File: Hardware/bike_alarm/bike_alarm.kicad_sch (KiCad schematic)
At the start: 4 parts, among them Q1 Q_NMOS_DGS, Y1 Piezo Buzzer

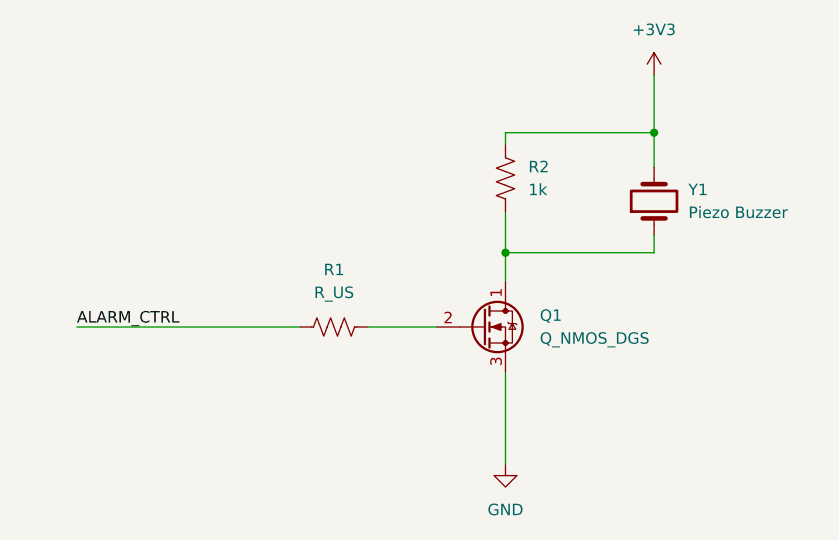
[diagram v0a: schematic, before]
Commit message: bike_alarm pcb update and bom
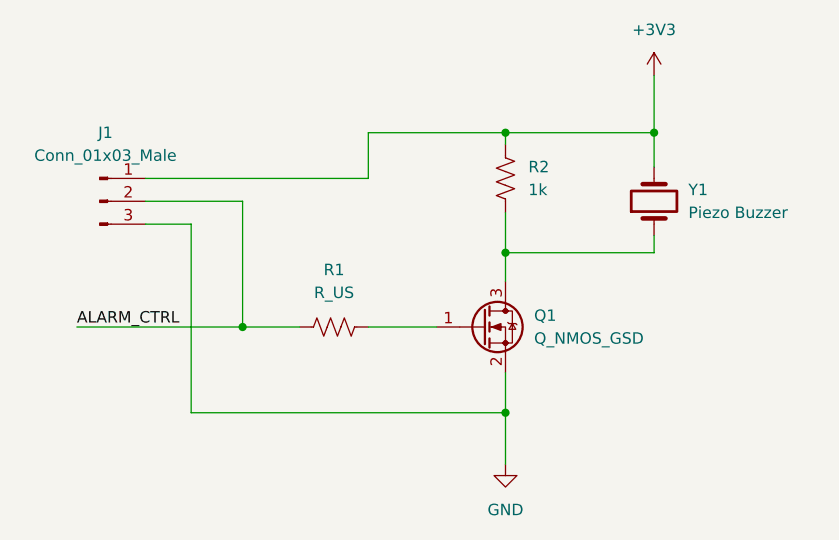
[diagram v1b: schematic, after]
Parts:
- removed Q1: Q_NMOS_DGS, Package_TO_SOT_SMD:SOT-23, symbol Device:Q_NMOS_DGS
- added J1: Conn_01x03_Male, Connector_PinHeader_2.54mm:PinHeader_1x03_P2.54mm_Vertical, symbol Connector:Conn_01x03_Male
- added Q1: Q_NMOS_GSD, Package_TO_SOT_SMD:SOT-23, symbol Device:Q_NMOS_GSD
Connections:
- net +3V3: now also J1.1 (Pin_1)
- net ALARM_CTRL: now also J1.2 (Pin_2)
- net GND: now also J1.3 (Pin_3), Q1.2 (S)
- net at R2.2, Y1.1: now also Q1.3 (D)
- net at R1.2: now also Q1.1 (G)
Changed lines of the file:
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@@
 (kicad_sch (version 20211123) (generator eeschema)
   (paper "A4")
+  (junction (at 81.28 108.585) (diameter 0) (color 0 0 0 0)
+  )
   (junction (at 81.28 90.805) (diameter 0) (color 0 0 0 0)
   )
+  (junction (at 52.07 99.06) (diameter 0) (color 0 0 0 0)
+  )
   (junction (at 97.79 77.47) (diameter 0) (color 0 0 0 0)
   )
-  (wire (pts (xy 81.28 104.14) (xy 81.28 114.3))
+  (junction (at 81.28 77.47) (diameter 0) (color 0 0 0 0)
+  )
+  (wire (pts (xy 41.275 87.63) (xy 46.355 87.63))
+    (stroke (width 0) (type default) (color 0 0 0 0))
+  )
+  (wire (pts (xy 41.275 85.09) (xy 52.07 85.09))
+    (stroke (width 0) (type default) (color 0 0 0 0))
+  )
+  (wire (pts (xy 41.275 82.55) (xy 66.04 82.55))
+    (stroke (width 0) (type default) (color 0 0 0 0))
+  )
+  (wire (pts (xy 81.28 104.14) (xy 81.28 108.585))
+    (stroke (width 0) (type default) (color 0 0 0 0))
+  )
+  (wire (pts (xy 52.07 85.09) (xy 52.07 99.06))
+    (stroke (width 0) (type default) (color 0 0 0 0))
+  )
+  (wire (pts (xy 46.355 108.585) (xy 81.28 108.585))
     (stroke (width 0) (type default) (color 0 0 0 0))
   )
@@
     (stroke (width 0) (type default) (color 0 0 0 0))
   )
+  (wire (pts (xy 81.28 108.585) (xy 81.28 114.3))
+    (stroke (width 0) (type default) (color 0 0 0 0))
+  )
   (wire (pts (xy 81.28 86.36) (xy 81.28 90.805))
     (stroke (width 0) (type default) (color 0 0 0 0))
   )
-  (wire (pts (xy 33.655 99.06) (xy 58.42 99.06))
+  (wire (pts (xy 33.655 99.06) (xy 52.07 99.06))
     (stroke (width 0) (type default) (color 0 0 0 0))
   )
@@
     (stroke (width 0) (type default) (color 0 0 0 0))
   )
+  (wire (pts (xy 52.07 99.06) (xy 58.42 99.06))
+    (stroke (width 0) (type default) (color 0 0 0 0))
+  )
+  (wire (pts (xy 66.04 77.47) (xy 81.28 77.47))
+    (stroke (width 0) (type default) (color 0 0 0 0))
+  )
   (wire (pts (xy 97.79 88.9) (xy 97.79 90.805))
     (stroke (width 0) (type default) (color 0 0 0 0))
   )
+  (wire (pts (xy 46.355 87.63) (xy 46.355 108.585))
+    (stroke (width 0) (type default) (color 0 0 0 0))
+  )
   (wire (pts (xy 81.28 77.47) (xy 97.79 77.47))
+    (stroke (width 0) (type default) (color 0 0 0 0))
+  )
+  (wire (pts (xy 66.04 82.55) (xy 66.04 77.47))
     (stroke (width 0) (type default) (color 0 0 0 0))
   )
@@
     (effects (font (size 1.27 1.27)) (justify left bottom))
   )
-  (symbol (lib_id "Device:Q_NMOS_DGS") (at 78.74 99.06 0) (unit 1)
-    (in_bom yes) (on_board yes) (fields_autoplaced)
-    (property "Reference" "Q1" (id 0) (at 85.09 97.7899 0)
-      (effects (font (size 1.27 1.27)) (justify left))
-    )
-    (property "Value" "Q_NMOS_DGS" (id 1) (at 85.09 100.3299 0)
+  (symbol (lib_id "Connector:Conn_01x03_Male") (at 36.195 85.09 0) (unit 1)
+    (in_bom yes) (on_board yes) (fields_autoplaced)
+    (property "Reference" "J1" (id 0) (at 36.83 77.47 0))
+    (property "Value" "Conn_01x03_Male" (id 1) (at 36.83 80.01 0))
+    (property "Footprint" "Connector_PinHeader_2.54mm:PinHeader_1x03_P2.54mm_Vertical" (id 2) (at 36.195 85.09 0)
+      (effects (font (size 1.27 1.27)) hide)
+    )
+    (property "Datasheet" "~" (id 3) (at 36.195 85.09 0)
+      (effects (font (size 1.27 1.27)) hide)
+    )
+    (pin "1")
+    (pin "2")
+    (pin "3")
+  )
+  (symbol (lib_id "Device:Q_NMOS_GSD") (at 78.74 99.06 0) (unit 1)
+    (in_bom yes) (on_board yes)
+    (property "Reference" "Q1" (id 0) (at 84.455 97.7899 0)
+      (effects (font (size 1.27 1.27)) (justify left))
+    )
+    (property "Value" "Q_NMOS_GSD" (id 1) (at 84.455 100.3299 0)
       (effects (font (size 1.27 1.27)) (justify left))
     )
@@
       (reference "#PWR0102") (unit 1) (value "GND") (footprint "")
     )
-    (path "/2d38429c-e76f-4ac3-a609-eca610b831a6"
-      (reference "Q1") (unit 1) (value "Q_NMOS_DGS") (footprint "Package_TO_SOT_SMD:SOT-23")
+    (path "/04c74dd5-f6c8-4c9d-8c28-3b17ac54986b"
+      (reference "J1") (unit 1) (value "Conn_01x03_Male") (footprint "Connector_PinHeader_2.54mm:PinHeader_1x03_P2.54mm_Vertical")
+    )
+    (path "/2da672a4-e8e8-42bd-b3a0-04b94e90287d"
+      (reference "Q1") (unit 1) (value "Q_NMOS_GSD") (footprint "Package_TO_SOT_SMD:SOT-23")
     )
     (path "/a1c19031-85a7-4245-9e0a-eed346ebf312"

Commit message: all boards pass DRC and have appropriate silkscreens, will order tomorrow
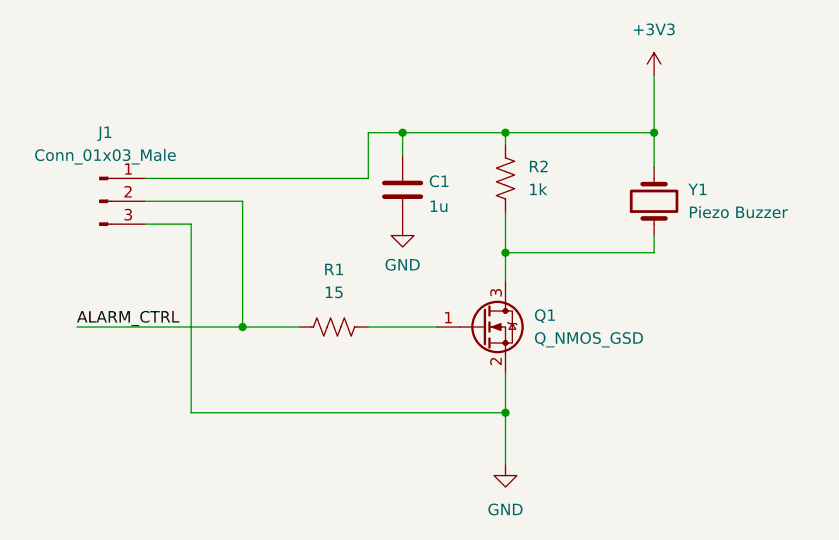
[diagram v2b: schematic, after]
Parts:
- added C1: 1u, Capacitor_SMD:C_0805_2012Metric, symbol Device:C
- R1: value R_US -> 15
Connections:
- net +3V3: now also C1.1
- net GND: now also C1.2
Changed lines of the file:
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@@
   (junction (at 81.28 77.47) (diameter 0) (color 0 0 0 0)
   )
+  (junction (at 69.85 77.47) (diameter 0) (color 0 0 0 0)
+  )
   (wire (pts (xy 41.275 87.63) (xy 46.355 87.63))
     (stroke (width 0) (type default) (color 0 0 0 0))
@@
     (stroke (width 0) (type default) (color 0 0 0 0))
   )
+  (wire (pts (xy 69.85 77.47) (xy 69.85 80.01))
+    (stroke (width 0) (type default) (color 0 0 0 0))
+  )
+  (wire (pts (xy 69.85 77.47) (xy 81.28 77.47))
+    (stroke (width 0) (type default) (color 0 0 0 0))
+  )
   (wire (pts (xy 97.79 77.47) (xy 97.79 81.28))
     (stroke (width 0) (type default) (color 0 0 0 0))
@@
     (stroke (width 0) (type default) (color 0 0 0 0))
   )
-  (wire (pts (xy 66.04 77.47) (xy 81.28 77.47))
+  (wire (pts (xy 66.04 77.47) (xy 69.85 77.47))
     (stroke (width 0) (type default) (color 0 0 0 0))
   )
@@
     (pin "3")
   )
+  (symbol (lib_id "power:GND") (at 69.85 87.63 0) (unit 1)
+    (in_bom yes) (on_board yes) (fields_autoplaced)
+    (property "Reference" "#PWR0103" (id 0) (at 69.85 93.98 0)
+      (effects (font (size 1.27 1.27)) hide)
+    )
+    (property "Value" "GND" (id 1) (at 69.85 92.1925 0))
+    (property "Footprint" "" (id 2) (at 69.85 87.63 0)
+      (effects (font (size 1.27 1.27)) hide)
+    )
+    (property "Datasheet" "" (id 3) (at 69.85 87.63 0)
+      (effects (font (size 1.27 1.27)) hide)
+    )
+    (pin "1")
+  )
   (symbol (lib_id "Device:Q_NMOS_GSD") (at 78.74 99.06 0) (unit 1)
     (in_bom yes) (on_board yes)
@@
     (pin "3")
   )
+  (symbol (lib_id "Device:C") (at 69.85 83.82 0) (unit 1)
+    (in_bom yes) (on_board yes) (fields_autoplaced)
+    (property "Reference" "C1" (id 0) (at 72.771 82.9115 0)
+      (effects (font (size 1.27 1.27)) (justify left))
+    )
+    (property "Value" "1u" (id 1) (at 72.771 85.6866 0)
+      (effects (font (size 1.27 1.27)) (justify left))
+    )
+    (property "Footprint" "Capacitor_SMD:C_0805_2012Metric" (id 2) (at 70.8152 87.63 0)
+      (effects (font (size 1.27 1.27)) hide)
+    )
+    (property "Datasheet" "~" (id 3) (at 69.85 83.82 0)
+      (effects (font (size 1.27 1.27)) hide)
+    )
+    (pin "1")
+    (pin "2")
+  )
   (symbol (lib_id "Device:R_US") (at 81.28 82.55 0) (unit 1)
     (in_bom yes) (on_board yes) (fields_autoplaced)
@@
     (in_bom yes) (on_board yes) (fields_autoplaced)
     (property "Reference" "R1" (id 0) (at 62.23 92.71 90))
-    (property "Value" "R_US" (id 1) (at 62.23 95.25 90))
+    (property "Value" "15" (id 1) (at 62.23 95.25 90))
     (property "Footprint" "Resistor_SMD:R_0805_2012Metric_Pad1.20x1.40mm_HandSolder" (id 2) (at 62.484 98.044 90)
       (effects (font (size 1.27 1.27)) hide)
@@
       (reference "#PWR0102") (unit 1) (value "GND") (footprint "")
     )
+    (path "/0e4abcd8-4868-4a30-91be-a7e9d224d533"
+      (reference "#PWR0103") (unit 1) (value "GND") (footprint "")
+    )
+    (path "/3b9b9b41-7b8e-4767-a0f4-b4622c8f5039"
+      (reference "C1") (unit 1) (value "1u") (footprint "Capacitor_SMD:C_0805_2012Metric")
+    )
     (path "/04c74dd5-f6c8-4c9d-8c28-3b17ac54986b"
       (reference "J1") (unit 1) (value "Conn_01x03_Male") (footprint "Connector_PinHeader_2.54mm:PinHeader_1x03_P2.54mm_Vertical")
@@
     )
     (path "/a1c19031-85a7-4245-9e0a-eed346ebf312"
-      (reference "R1") (unit 1) (value "R_US") (footprint "Resistor_SMD:R_0805_2012Metric_Pad1.20x1.40mm_HandSolder")
+      (reference "R1") (unit 1) (value "15") (footprint "Resistor_SMD:R_0805_2012Metric_Pad1.20x1.40mm_HandSolder")
     )
     (path "/60fabe2e-c18d-4d49-8460-7dcfca564713"
